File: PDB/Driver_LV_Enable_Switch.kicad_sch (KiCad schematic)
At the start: 6 parts, among them J5 Driver_LV_Enable_Switch, Q1 DTC144EU3HZGT106, Q5 Q_PMOS_GSD

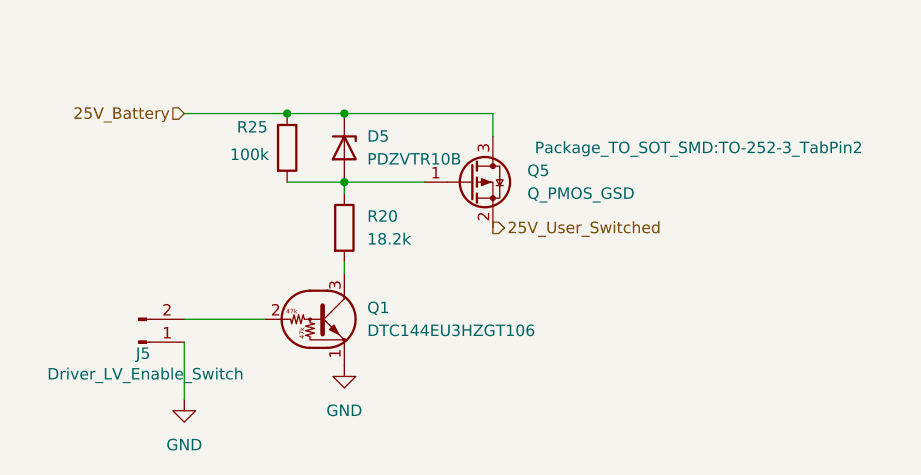
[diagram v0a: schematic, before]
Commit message: sry forgot to push, waiting on PCB shipping atm. Notes: split power distribution into two boards, one for the main 25V distribution, and another for 12V stuff. Also updated CAN transciever. the previous one was a 5V logic one (same logic as its power), and would have fried our ESPs data pins
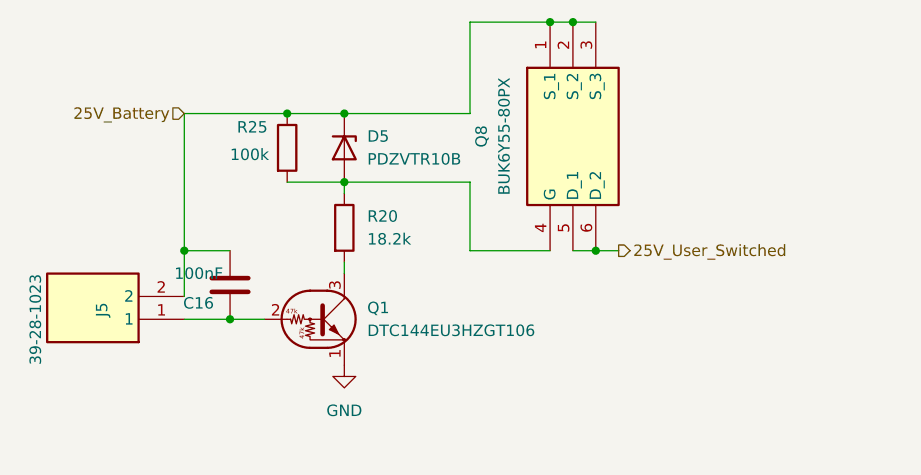
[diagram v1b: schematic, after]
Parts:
- removed J5: Driver_LV_Enable_Switch, PROVE-footprints:TE_1877285-2, symbol Connector:Conn_01x02_Pin
- removed Q5: Q_PMOS_GSD, Package_TO_SOT_SMD:TO-252-3_TabPin2, symbol Transistor_FET:Q_PMOS_GSD
- added C16: 100nF, Capacitor_SMD:C_0805_2012Metric_Pad1.18x1.45mm_HandSolder, symbol PROVE:1206B104K500CT
- added J5: 39-28-1023, PROVE-footprints:39-28-1023, symbol PROVE_Symbols:39-28-1023
- added Q8: BUK6Y55-80PX, PROVE-footprints:BUK6Y55-80PX, symbol PROVE_Symbols:BUK6Y55-80PX
- Q1: Purchase Link (none) -> https://www.mouser.com/en/ProductDetail/ROHM-Semiconductor/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
- R20: footprint Resistor_SMD:R_1206_3216Metric_Pad1.30x1.75mm_HandSolder -> Resistor_SMD:R_0805_2012Metric_Pad1.20x1.40mm_HandSolder; Purchase Link https://www.mouser.com/en/ProductDetail/Vishay/CRCW120618K2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 -> https://www.mouser.com/en/ProductDetail/Vishay/CRCW080518K2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; Specs Resistance: 18.2 kΩ. Tolerance: 1.0% Power: 250 mW -> 18.2 kΩ, ±1%
- R25: footprint Resistor_SMD:R_1206_3216Metric_Pad1.30x1.75mm_HandSolder -> Resistor_SMD:R_0805_2012Metric_Pad1.20x1.40mm_HandSolder; Purchase Link https://www.mouser.com/en/ProductDetail/KOA-Speer/RK73H2BTT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 -> https://www.mouser.com/en/ProductDetail/Vishay/CRCW0805100K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; Specs (none) -> 100 kΩ, ±1%, AEC-Q200
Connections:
- net 25V_Battery: now also C16.1, J5.2, Q8.1 (S_1), Q8.2 (S_2), Q8.3 (S_3)
- net 25V_User_Switched: now also Q8.5 (D_1), Q8.6 (D_2)
- net at Q1.2 (B): now also C16.2, J5.1
- net at D5.2 (A), R20.1, R25.2: now also Q8.4 (G)
